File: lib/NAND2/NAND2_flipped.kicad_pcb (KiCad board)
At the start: 2 copper layers, 4 parts

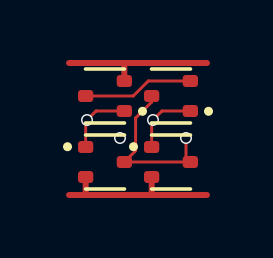
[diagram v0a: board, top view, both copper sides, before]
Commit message: Rename NAND into NAND2 and its inputs A and B into A1 and A2 (general convention when the pins can be swapped)
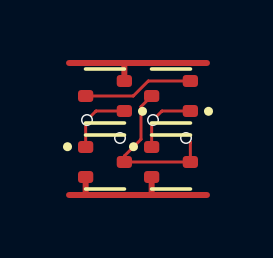
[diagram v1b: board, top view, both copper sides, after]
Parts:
- moved N1 2.20 mm to (1.10, 1.10), turned to 180 degrees
- moved N2 2.20 mm to (3.30, 1.10), turned to 180 degrees
- moved P1 2.20 mm to (1.10, 3.30), turned to 0 degrees
- moved P2 2.20 mm to (3.30, 3.30), turned to 0 degrees
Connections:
- net A renamed A1
- net B renamed A2
- N1 pad 3: Y -> int1
- N2 pad 2: GND -> int1
- P1 pad 3: C -> Y
- P2 pad 2: C -> VDD
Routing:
- net int1: track 0.00 -> 3.70 mm
- net C: track 3.70 -> 0.00 mm
- net a910: track 0.00 -> 2.29 mm, vias 0 -> 1
- net A1: track 2.29 -> 0.00 mm, vias 1 -> 0
- net VDD: track 5.19 -> 5.80 mm
- net GND: track 5.80 -> 5.20 mm

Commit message: All cells now use 1mm*4mm grid rather than 1.1mm*4.4mm
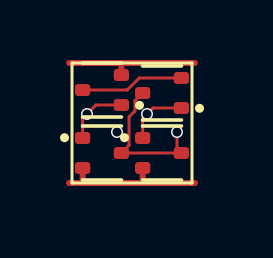
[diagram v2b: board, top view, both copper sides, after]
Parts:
- moved P2 0.42 mm to (3.00, 3.00)
- moved N2 0.32 mm to (3.00, 1.00)
- moved P1 0.32 mm to (1.00, 3.00)
- moved N1 0.22 mm to (1.00, 0.90)
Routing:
- net a910: track 2.29 -> 0.00 mm, vias 1 -> 0
- net A1: track 0.00 -> 2.13 mm, vias 0 -> 1
- net VDD: track 5.80 -> 5.11 mm
- net Y: track 5.64 -> 5.05 mm
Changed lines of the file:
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@@
 	(net 1 "Y")
 	(net 2 "GND")
-	(net 3 "a910")
+	(net 3 "A1")
 	(net 4 "VDD")
 	(net 5 "int1")
@@
 	(footprint "Package_TO_SOT_SMD:SOT-523"
 		(layer "F.Cu")
-		(at 3.3 1.1 180)
+		(at 3 1 180)
 		(descr "SOT523, https://www.diodes.com/assets/Package-Files/SOT523.pdf")
 		(tags "SOT-523")
@@
 	(footprint "Package_TO_SOT_SMD:SOT-523"
 		(layer "F.Cu")
-		(at 3.3 3.3)
+		(at 3 3)
 		(descr "SOT523, https://www.diodes.com/assets/Package-Files/SOT523.pdf")
 		(tags "SOT-523")
@@
 	(footprint "Package_TO_SOT_SMD:SOT-523"
 		(layer "F.Cu")
-		(at 1.1 1.1 180)
+		(at 1 0.9 180)
 		(descr "SOT523, https://www.diodes.com/assets/Package-Files/SOT523.pdf")
 		(tags "SOT-523")
@@
 	(footprint "Package_TO_SOT_SMD:SOT-523"
 		(layer "F.Cu")
-		(at 1.1 3.3)
+		(at 1 3)
 		(descr "SOT523, https://www.diodes.com/assets/Package-Files/SOT523.pdf")
 		(tags "SOT-523")
@@
 		)
 	)
+	(gr_rect
+		(start 0 0)
+		(end 4 4)
+		(stroke
+			(width 0.1)
+			(type default)
+		)
+		(fill no)
+		(layer "F.SilkS")
+	)
 	(via
-		(at 1.6 2.5)
+		(at 1.5 2.3)
 		(size 0.4)
 		(drill 0.3)
@@
 	)
 	(segment
-		(start 1.745 3.3)
-		(end 1.745 3.100001)
+		(start 3.5 2.3)
+		(end 3.5 2.855)
 		(width 0.1)
 		(layer "F.Cu")
@@
 	)
 	(segment
-		(start 1.745 3.100001)
-		(end 2.3 2.545001)
+		(start 2.099 1.601)
+		(end 2.099 1.256)
 		(width 0.1)
 		(layer "F.Cu")
@@
 	)
 	(segment
-		(start 2.3 1.455)
-		(end 2.655 1.1)
+		(start 1.645 3)
+		(end 1.901 2.744)
 		(width 0.1)
 		(layer "F.Cu")
@@
 	)
 	(segment
-		(start 2.3 2.545001)
-		(end 2.3 1.455)
+		(start 3.5 2.855)
+		(end 3.645 3)
 		(width 0.1)
 		(layer "F.Cu")
@@
 	)
 	(segment
-		(start 3.945 3.3)
-		(end 1.745 3.3)
+		(start 1.901 2.744)
+		(end 1.901 1.799)
 		(width 0.1)
 		(layer "F.Cu")
@@
 	)
 	(segment
-		(start 3.945 2.645)
-		(end 3.8 2.5)
+		(start 2.099 1.256)
+		(end 2.355 1)
 		(width 0.1)
 		(layer "F.Cu")
@@
 	)
 	(segment
-		(start 3.945 3.3)
-		(end 3.945 2.645)
+		(start 3.645 3)
+		(end 1.645 3)
 		(width 0.1)
 		(layer "F.Cu")
 		(net 1)
 	)
+	(segment
+		(start 1.901 1.799)
+		(end 2.099 1.601)
+		(width 0.1)
+		(layer "F.Cu")
+		(net 1)
+	)
 	(via
-		(at 3.8 2.5)
+		(at 3.5 2.3)
 		(size 0.4)
 		(drill 0.3)
@@
 	)
 	(segment
-		(start 1.745 0.6)
-		(end 1.745 0.005)
+		(start 1.6 0)
+		(end 1.75 0)
 		(width 0.2)
 		(layer "F.Cu")
@@
 	)
 	(segment
+		(start 1.645 0.045)
+		(end 1.6 0)
+		(width 0.2)
+		(layer "F.Cu")
+		(net 2)
+	)
+	(segment
+		(start 1.645 0.5)
+		(end 1.645 0.045)
+		(width 0.2)
+		(layer "F.Cu")
+		(net 2)
+	)
+	(segment
 		(start -0.1 0)
-		(end 1.75 0)
+		(end 1.6 0)
 		(width 0.2)
 		(layer "F.Cu")
@@
 	(segment
 		(start 1.75 0)
-		(end 4.5 0)
+		(end 4.1 0)
 		(width 0.2)
 		(layer "F.Cu")
@@
 	)
 	(segment
-		(start 0.455 2.8)
-		(end 0.455 1.945)
+		(start 1.645 1.4)
+		(end 0.8 1.4)
 		(width 0.1)
 		(layer "F.Cu")
@@
 	)
 	(segment
-		(start 0.455 1.945)
-		(end 0.5 1.9)
+		(start 0.355 2.5)
+		(end 0.355 1.845)
 		(width 0.1)
 		(layer "F.Cu")
@@
 	)
 	(segment
-		(start 1.745 1.6)
-		(end 0.8 1.6)
+		(start 0.355 1.845)
+		(end 0.5 1.7)
 		(width 0.1)
 		(layer "F.Cu")
@@
 	)
 	(segment
-		(start 0.8 1.6)
-		(end 0.5 1.9)
+		(start 0.8 1.4)
+		(end 0.5 1.7)
 		(width 0.1)
 		(layer "F.Cu")
@@
 	)
 	(via
-		(at 0.5 1.9)
+		(at 0.5 1.7)
 		(size 0.4)
 		(drill 0.3)
@@
 	)
 	(segment
-		(start 2.65 4.4)
-		(end 4.5 4.4)
+		(start 2.355 3.5)
+		(end 2.355 3.955)
 		(width 0.2)
 		(layer "F.Cu")
@@
 	)
 	(segment
-		(start 0.46 4.4)
-		(end 2.65 4.4)
+		(start 2.65 4)
+		(end 4.1 4)
 		(width 0.2)
 		(layer "F.Cu")
@@
 	)
 	(segment
-		(start 2.655 4.395)
-		(end 2.65 4.4)
+		(start 0.355 3.5)
+		(end 0.355 3.895)
 		(width 0.2)
 		(layer "F.Cu")
@@
 	)
 	(segment
-		(start 2.655 3.8)
-		(end 2.655 4.395)
+		(start 0.46 4)
+		(end 2.4 4)
 		(width 0.2)
 		(layer "F.Cu")
@@
 	)
 	(segment
-		(start 0.455 3.8)
-		(end 0.455 4.395)
+		(start 2.4 4)
+		(end 2.65 4)
 		(width 0.2)
 		(layer "F.Cu")
@@
 	)
 	(segment
-		(start -0.1 4.4)
-		(end 0.46 4.4)
+		(start -0.1 4)
+		(end 0.46 4)
 		(width 0.2)
 		(layer "F.Cu")
@@
 	)
 	(segment
-		(start 0.455 4.395)
-		(end 0.46 4.4)
+		(start 2.355 3.955)
+		(end 2.4 4)
 		(width 0.2)
 		(layer "F.Cu")
@@
 	)
 	(segment
-		(start 2.542262 0.6)
-		(end 2.042262 1.1)
+		(start 0.355 0.9)
+		(end 1.842262 0.9)
 		(width 0.1)
 		(layer "F.Cu")
@@
 	)
 	(segment
-		(start 3.945 0.6)
-		(end 2.542262 0.6)
+		(start 1.842262 0.9)
+		(end 2.242262 0.5)
 		(width 0.1)
 		(layer "F.Cu")
@@
 	)
 	(segment
-		(start 2.042262 1.1)
-		(end 0.455 1.1)
+		(start 2.242262 0.5)
+		(end 3.645 0.5)
 		(width 0.1)
 		(layer "F.Cu")
@@
 	)
 	(segment
-		(start 3 1.6)
-		(end 2.7 1.9)
+		(start 2.7 1.5)
+		(end 2.5 1.7)
 		(width 0.1)
 		(layer "F.Cu")
@@
 	)
 	(segment
-		(start 2.655 1.945)
-		(end 2.7 1.9)
+		(start 2.355 1.845)
+		(end 2.5 1.7)
 		(width 0.1)
 		(layer "F.Cu")
@@
 	)
 	(segment
-		(start 2.655 2.8)
-		(end 2.655 1.945)
+		(start 3.645 1.5)
+		(end 2.7 1.5)
 		(width 0.1)
 		(layer "F.Cu")
@@
 	)
 	(segment
-		(start 3.945 1.6)
-		(end 3 1.6)
+		(start 2.355 2.5)
+		(end 2.355 1.845)
 		(width 0.1)
 		(layer "F.Cu")
@@
 	)
 	(via
-		(at 2.7 1.9)
+		(at 2.5 1.7)
 		(size 0.4)
 		(drill 0.3)

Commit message: Make the pads of my SOT523 footprint very slightly smaller, which is enough to route all the cells and leave the mosfets exactly on the grid
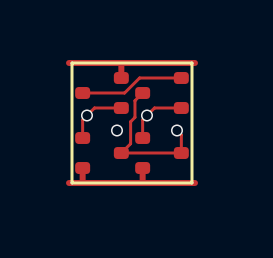
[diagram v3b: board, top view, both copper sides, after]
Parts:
- N1, N2, P1, P2: footprint Package_TO_SOT_SMD:SOT-523 -> RV523:SOT523
- moved N1 0.10 mm to (1.00, 1.00)

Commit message: Propagate MOSFET values to the cells' PCBs
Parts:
- N1, N2: value (none) -> NMOS
- P1, P2: value (none) -> PMOS
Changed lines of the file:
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@@
 			)
 		)
-		(property "Value" ""
+		(property "Value" "NMOS"
 			(at 0 0 180)
 			(layer "F.Fab")
@@
 			)
 		)
-		(property "Value" ""
+		(property "Value" "PMOS"
 			(at 0 0 0)
 			(layer "F.Fab")
@@
 			)
 		)
-		(property "Value" ""
+		(property "Value" "NMOS"
 			(at 0 0 180)
 			(layer "F.Fab")
@@
 			)
 		)
-		(property "Value" ""
+		(property "Value" "PMOS"
 			(at 0 0 0)
 			(layer "F.Fab")
